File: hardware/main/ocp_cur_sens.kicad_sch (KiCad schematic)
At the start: 45 parts, among them U10 TL331, U11 TL331, U13 74LVC1G11, U2 INA181, U3 INA181, U4 INA181, U8 LMV321, U9 TL331

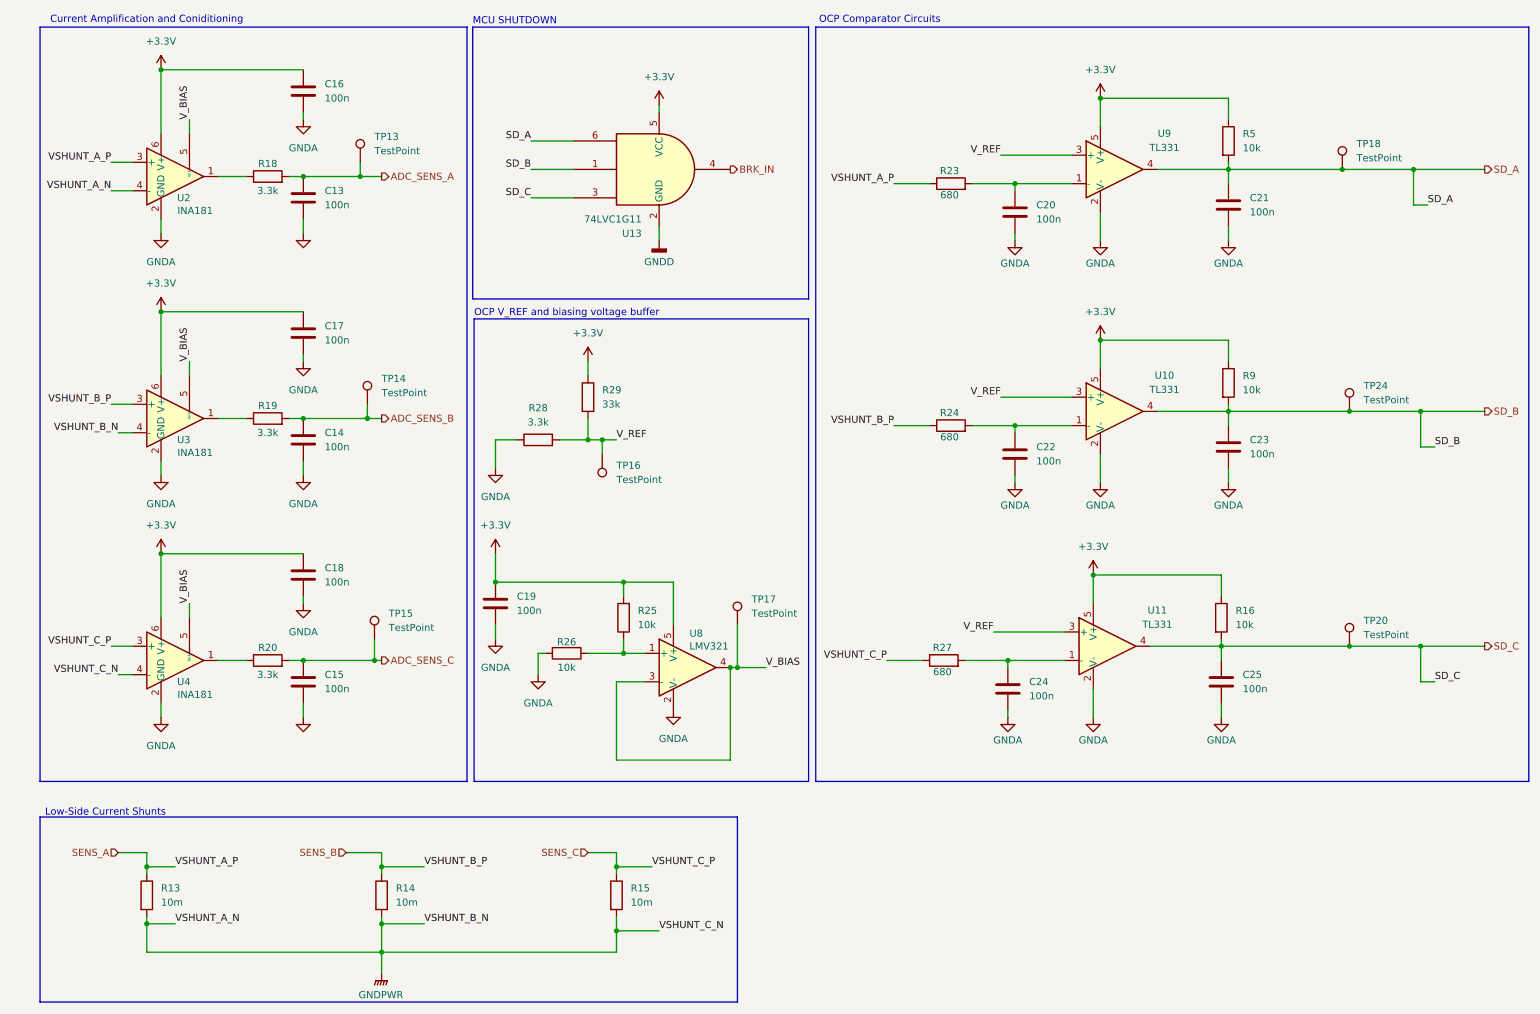
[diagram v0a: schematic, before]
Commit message: added status LED's to schema, fixed gate drive error, added BOM
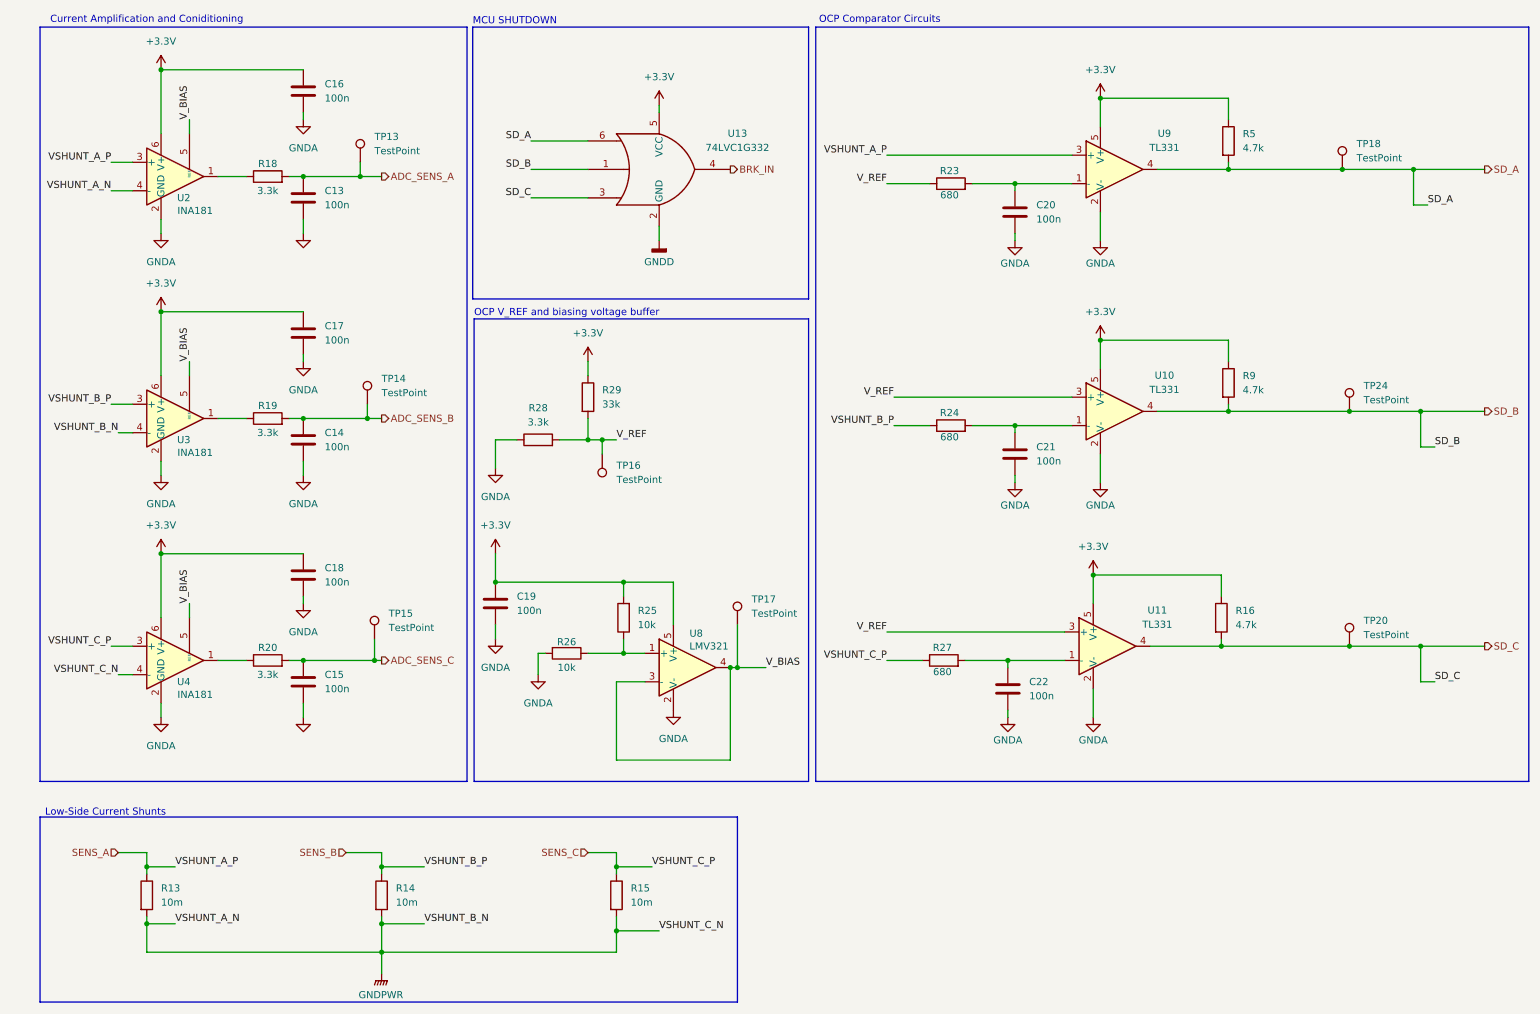
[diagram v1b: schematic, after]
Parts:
- removed C23, C24, C25: 100n, Capacitor_SMD:C_0402_1005Metric_Pad0.74x0.62mm_HandSolder, symbol Device:C
- removed U13: 74LVC1G11, symbol 74xGxx:74LVC1G11
- added U13: 74LVC1G332, footprint:MURA160T3G, symbol 74xGxx:74LVC1G332
- C13, C14, C15, C16, C17, C18, C19, C20, C21, C22: footprint Capacitor_SMD:C_0402_1005Metric_Pad0.74x0.62mm_HandSolder -> Capacitor_SMD:C_0603_1608Metric
- R13, R14, R15: footprint Resistor_SMD:R_2512_6332Metric_Pad1.40x3.35mm_HandSolder -> Resistor_SMD:R_2512_6332Metric
- R16, R5, R9: value 10k -> 4.7k; footprint (none) -> Resistor_SMD:R_0603_1608Metric
- R18, R19, R20, R23, R24, R25, R26, R27, R28, R29: footprint (none) -> Resistor_SMD:R_0603_1608Metric
- TP13, TP14, TP15, TP16, TP17, TP18, TP20, TP24: footprint (none) -> TestPoint:TestPoint_Pad_1.5x1.5mm
- U8: footprint (none) -> footprint:LMV321DBV5
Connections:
- net +3.3V: now also U13.5 (VCC)
- net BRK_IN: now also U13.4
- net GNDD: now also U13.2 (GND)
- net SD_A: now also U13.6; no longer C21.1
- net SD_B: now also U13.1
- net SD_C: now also U13.3
- net SENS_A: now also U9.3 (+); no longer R23.1
- net V_REF: now also R23.1; no longer U9.3 (+)
- net at R24.2, U10.1 (-): now also C21.1; no longer C22.1
- net at R27.2, U11.1 (-): now also C22.1

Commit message: hardware layout started
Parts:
- TP13, TP14, TP15, TP16, TP17, TP18, TP20: footprint TestPoint:TestPoint_Pad_1.5x1.5mm -> TestPoint:TestPoint_Pad_D1.5mm
- U13: footprint footprint:MURA160T3G -> footprint:74LVC1G332_DCK0006A_N
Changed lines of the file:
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@@
 			)
 		)
-		(property "Footprint" "TestPoint:TestPoint_Pad_1.5x1.5mm"
+		(property "Footprint" "TestPoint:TestPoint_Pad_D1.5mm"
 			(at 78.74 44.45 0)
 			(hide yes)
@@
 			)
 		)
-		(property "Footprint" "TestPoint:TestPoint_Pad_1.5x1.5mm"
+		(property "Footprint" "TestPoint:TestPoint_Pad_D1.5mm"
 			(at 254 45.72 0)
 			(hide yes)
@@
 			)
 		)
-		(property "Footprint" "footprint:MURA160T3G"
+		(property "Footprint" "footprint:74LVC1G332_DCK0006A_N"
 			(at 127 45.72 0)
 			(hide yes)
@@
 			)
 		)
-		(property "Footprint" "TestPoint:TestPoint_Pad_1.5x1.5mm"
+		(property "Footprint" "TestPoint:TestPoint_Pad_D1.5mm"
 			(at 80.01 87.63 0)
 			(hide yes)
@@
 			)
 		)
-		(property "Footprint" "TestPoint:TestPoint_Pad_1.5x1.5mm"
+		(property "Footprint" "TestPoint:TestPoint_Pad_D1.5mm"
 			(at 146.05 127 0)
 			(hide yes)
@@
 			)
 		)
-		(property "Footprint" "TestPoint:TestPoint_Pad_1.5x1.5mm"
+		(property "Footprint" "TestPoint:TestPoint_Pad_D1.5mm"
 			(at 111.76 96.52 0)
 			(hide yes)
@@
 			)
 		)
-		(property "Footprint" "TestPoint:TestPoint_Pad_1.5x1.5mm"
+		(property "Footprint" "TestPoint:TestPoint_Pad_D1.5mm"
 			(at 81.28 129.54 0)
 			(hide yes)
@@
 			)
 		)
-		(property "Footprint" "TestPoint:TestPoint_Pad_1.5x1.5mm"
+		(property "Footprint" "TestPoint:TestPoint_Pad_D1.5mm"
 			(at 255.27 130.81 0)
 			(hide yes)
